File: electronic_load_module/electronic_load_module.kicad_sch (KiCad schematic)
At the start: 71 parts, among them J1 Conn_01x03_Pin, J10 Conn_01x02_Pin, J2 Conn_01x03_Pin, J2 Screw_Terminal_01x02, J3 Conn_01x04_Pin, J6 Conn_01x05_Pin, J7 Conn_01x04_Pin, J8 Conn_01x04_Pin, J9 Conn_01x04_Pin, Q1 TIP142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

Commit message: Image added
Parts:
- V1: now not fitted; now left out of the parts list
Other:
- moved on the sheet: C1, C2, C4, C5, C6, C8, J3, J7, Q2, Q3, R11, R5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

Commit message: IDeo ok
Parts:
- removed C4, C8: 100n, Capacitor_SMD:C_0603_1608Metric_Pad1.08x0.95mm_HandSolder, symbol Device:C
- removed J1: Conn_01x03_Pin, Connector_PinHeader_2.54mm:PinHeader_1x03_P2.54mm_Vertical, symbol Connector:Conn_01x03_Pin
- removed J10: Conn_01x02_Pin, Connector_PinHeader_2.54mm:PinHeader_1x02_P2.54mm_Vertical, symbol Connector:Conn_01x02_Pin
- removed J2: Screw_Terminal_01x02, TerminalBlock:TerminalBlock_Altech_AK300-2_P5.00mm, symbol Connector:Screw_Terminal_01x02
- removed J3, J7, J8, J9: Conn_01x04_Pin, Connector_PinHeader_2.54mm:PinHeader_1x04_P2.54mm_Vertical, symbol Connector:Conn_01x04_Pin
- removed Q3, Q4: BC549, Package_TO_SOT_THT:TO-92_Inline, symbol SPICE_bjts:BC549
- removed R11: 280k, Resistor_SMD:R_0603_1608Metric_Pad0.98x0.95mm_HandSolder, symbol Device:R
- removed R11: 20k, Resistor_SMD:R_0603_1608Metric_Pad0.98x0.95mm_HandSolder, symbol Device:R
- removed R5 (x17): 0, Resistor_SMD:R_0603_1608Metric_Pad0.98x0.95mm_HandSolder, symbol Device:R
- removed R5 (x3): 10k, Resistor_SMD:R_0603_1608Metric_Pad0.98x0.95mm_HandSolder, symbol Device:R
- removed R5 (x2): 1k, Resistor_SMD:R_0603_1608Metric_Pad0.98x0.95mm_HandSolder, symbol Device:R
- removed unit 2 of U1
- removed unit 5 of U1
- removed unit 3 of U1
- removed unit 4 of U1
- removed U2: MCP9700Ax-ETT, Package_TO_SOT_THT:TO-92_Inline, symbol Sensor_Temperature:MCP9700Ax-ETT
- removed unit 1 of U6
- removed V1: 5, symbol Simulation_SPICE:VDC
- added C9 (x3): 100n, Capacitor_SMD:C_0603_1608Metric_Pad1.08x0.95mm_HandSolder, symbol Device:C
- added J10: Conn_01x05_Pin, Connector_JST:JST_EH_B5B-EH-A_1x05_P2.50mm_Vertical, symbol Connector:Conn_01x05_Pin
- added J11: Conn_01x03_Pin, Connector_PinHeader_2.54mm:PinHeader_1x03_P2.54mm_Vertical, symbol Connector:Conn_01x03_Pin
- added J5, J7: Conn_01x03_Pin, Connector_JST:JST_EH_B3B-EH-A_1x03_P2.50mm_Vertical, symbol Connector:Conn_01x03_Pin
- added J8, J9: Conn_01x02_Socket, Connector_JST:JST_EH_B2B-EH-A_1x02_P2.50mm_Vertical, symbol Connector:Conn_01x02_Socket
- added R11: 90k, Resistor_SMD:R_0603_1608Metric_Pad0.98x0.95mm_HandSolder, symbol Device:R
- added R11: 100, Resistor_SMD:R_0603_1608Metric_Pad0.98x0.95mm_HandSolder, symbol Device:R
- added R11: 3.3k, Resistor_SMD:R_0603_1608Metric_Pad0.98x0.95mm_HandSolder, symbol Device:R
- added R11: 6.6k, Resistor_SMD:R_0603_1608Metric_Pad0.98x0.95mm_HandSolder, symbol Device:R
- added R5: 10k, Resistor_SMD:R_0603_1608Metric_Pad0.98x0.95mm_HandSolder, symbol Device:R
- added U2: TLV07, Package_SO:SOIC-8_3.9x4.9mm_P1.27mm, symbol SPICE_opamps:TLV07
- B1, J2, V2, V6: now not fitted; now left out of the parts list
- C2, C7: value 10n -> 100p
- J6: footprint Connector_PinHeader_2.54mm:PinHeader_1x05_P2.54mm_Vertical -> Connector_JST:JST_EH_B5B-EH-A_1x05_P2.50mm_Vertical; Price (none) -> 0.02
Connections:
- net ADC_SHUNT is gone; now on an unnamed net: J2.2 (Pin_2)
- net ADC_SHUNT_2 is gone; now on an unnamed net: U6.14
- net TEMP is gone; now on net COMMON_MUX_B: J6.3 (Pin_3)
- net input_divider is gone; now on an unnamed net: U1.3 (+)
- net 0: now also J6.5 (Pin_5), C9.2, C9.2, C9.2, J10.5 (Pin_5), R5.1, U2.4 (V-)
- net 5V: now also J6.1 (Pin_1), C9.1, C9.1, C9.1, J10.1 (Pin_1), U2.7 (V+)
- net COMMON_MUX_A: now also J6.2 (Pin_2), J10.2 (Pin_2); no longer J6.1 (Pin_1)
- net COMMON_MUX_B: now also J10.3 (Pin_3); no longer J6.2 (Pin_2)
- net DAC: now also U3.2 (Y2), U6.7, J11.1 (Pin_1)
- net DAC_2: now also J2.1 (Pin_1), U5.2 (Y2), U6.8, R5.2; no longer U6.7
- net DAC_from_board: now also J8.1 (Pin_1); no longer J2.1 (Pin_1)
- net DAC_from_board_2: now also J9.1 (Pin_1)
- net DIVIDER: now also U3.15 (X2), U5.15 (X2), J10.4 (Pin_4), U2.2 (-), U2.6; no longer J6.5 (Pin_5), U1.1
- net SHUNT: now also U3.4 (Y3), U3.5 (Y1), J8.2 (Pin_2)
- net SHUNT_2: now also U5.4 (Y3), U5.5 (Y1), J9.2 (Pin_2); no longer U6.12 (+)
- net input_sense: now also J7.1 (Pin_1), R11.1
- net at C7.1, R5.2: now also U6.10 (+); no longer U6.5 (+)
- net at U1.2 (-): now also C1.1, R5.2, U3.3 (Y)
- net at U6.13 (-): now also C5.1, R5.2, U5.3 (Y)
- net at U5.14 (X1): now also U5.11 (X3)
- net at U5.13 (X): now also U6.12 (+); no longer U6.10 (+)
- net at R5.1: now also U6.6 (-)
- net at C5.2, R5.1: no longer U6.8
- net at U3.14 (X1): now also U3.11 (X3), J11.2 (Pin_2)
- net at C2.1, R5.2: now also U6.5 (+)
- net at C1.2, R5.1: now also U1.1
- net at R5.1: now also U6.9 (-); no longer U6.6 (-)
- net ENABLE renamed MIXER
- net MIXER: now also J11.3 (Pin_3), J5.3 (Pin_3)
- new net: J7.3 (Pin_3), R11.2
- new net DIVIDER_R: R11.1, R11.2, U2.3 (+)
- new net input_10: J5.1 (Pin_1), R11.1, R11.2
- new net input_1000: J5.2 (Pin_2), R11.1, R11.2
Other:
- note added: "BJT half"
- note added: "Connector to mixer"
- note added: "Connectors to front panel"
- note added: "Daisy chain"
- note added: "jumpers used to select DAC or MIXER control"
- note added: "omit on the rest of the modules"
- note removed: "10 mV/C"
- note removed: "50 kHz reguliše prilično dobro"
- note removed: "ADD ENABLE"
- note removed: "drop ovog tranzistora je 2V na 8A, strava."
- note removed: "https://novi.kupujemprodajem.com/elektronika-i-komponente/moduli-za-samoizgradnju/mcp4725-i2c-dac-12-bitni-modul/oglas/137304825?filterId=3854618127 Jednom zameniće DAC"
- note removed: "leave blank for additonal modules"
- note removed: "možda dodati ako bi se trimovao offset i gain error koji unosi 1% otpornik."
- note removed: "napajanje će biti neki mali flyback, vrv oni noisy adapteri, treba videti koliko bi šumili"
- note removed: "tlv9061 osetvljiv na promena input napona"
- note removed: "to_control daisy chain"
- moved on the sheet: C1, C2, C3, C5, C6, C7, C9, Q1, Q2, R11, R5, U3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

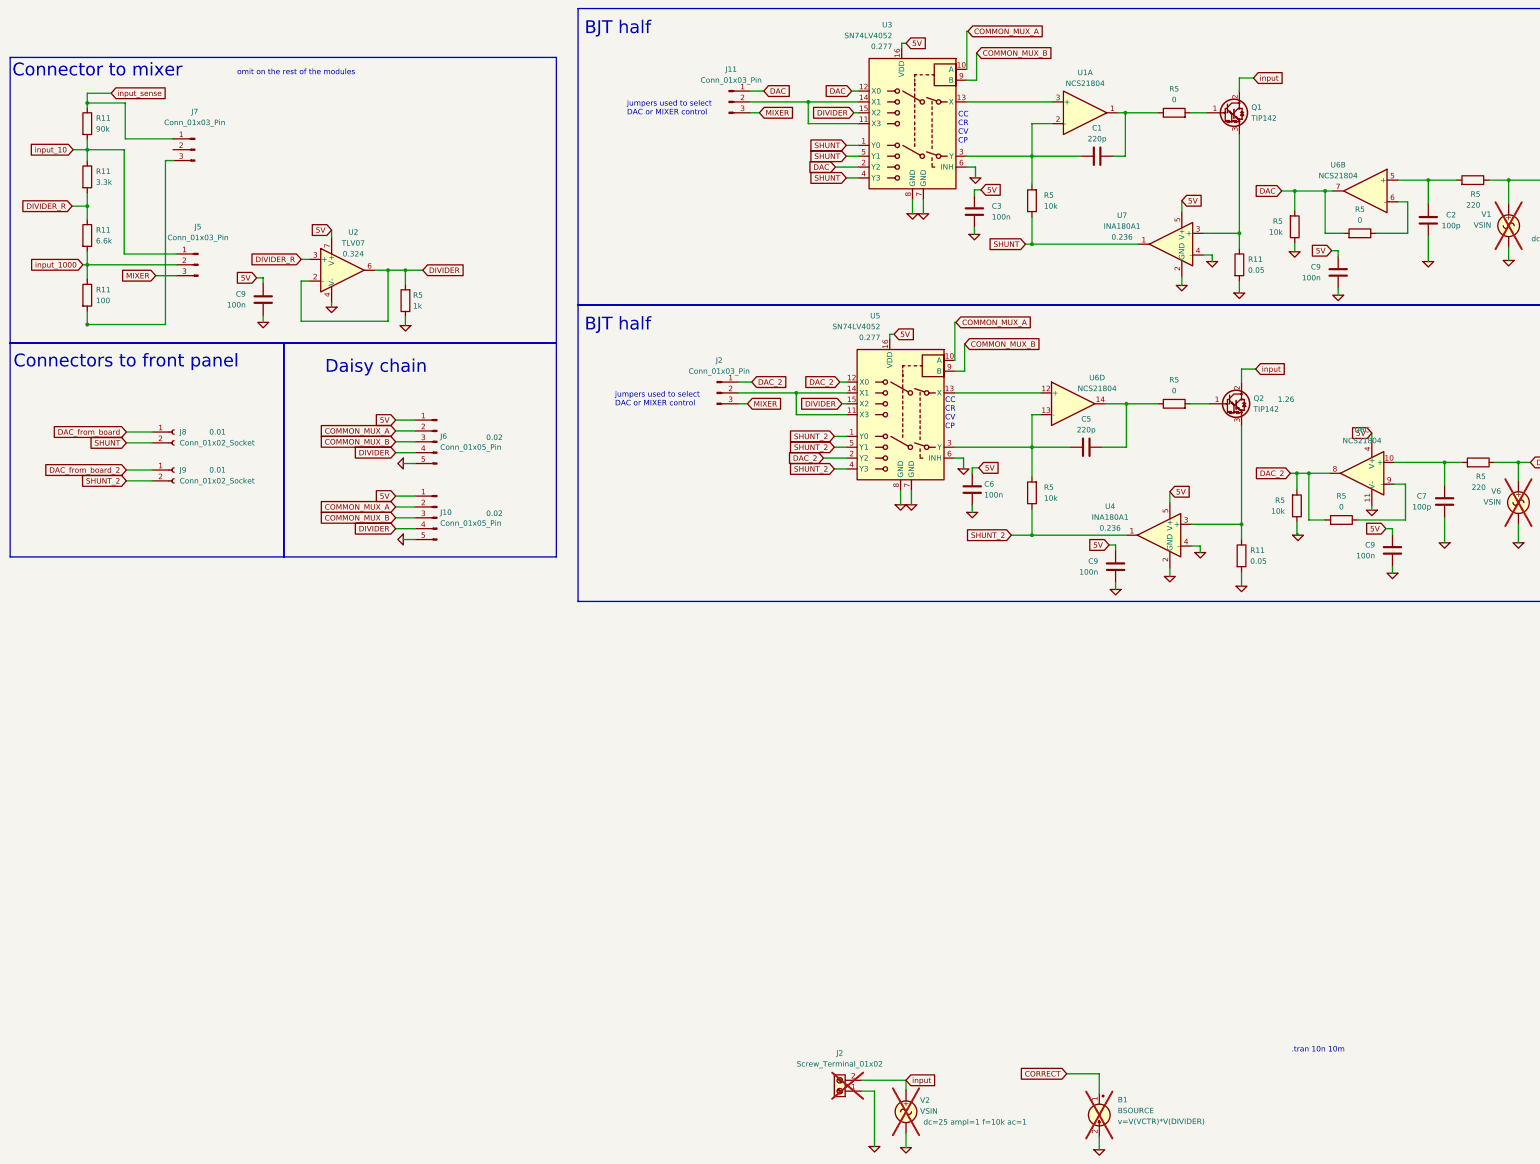
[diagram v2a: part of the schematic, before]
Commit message: Konačno PCB za BJT modul je počeo.
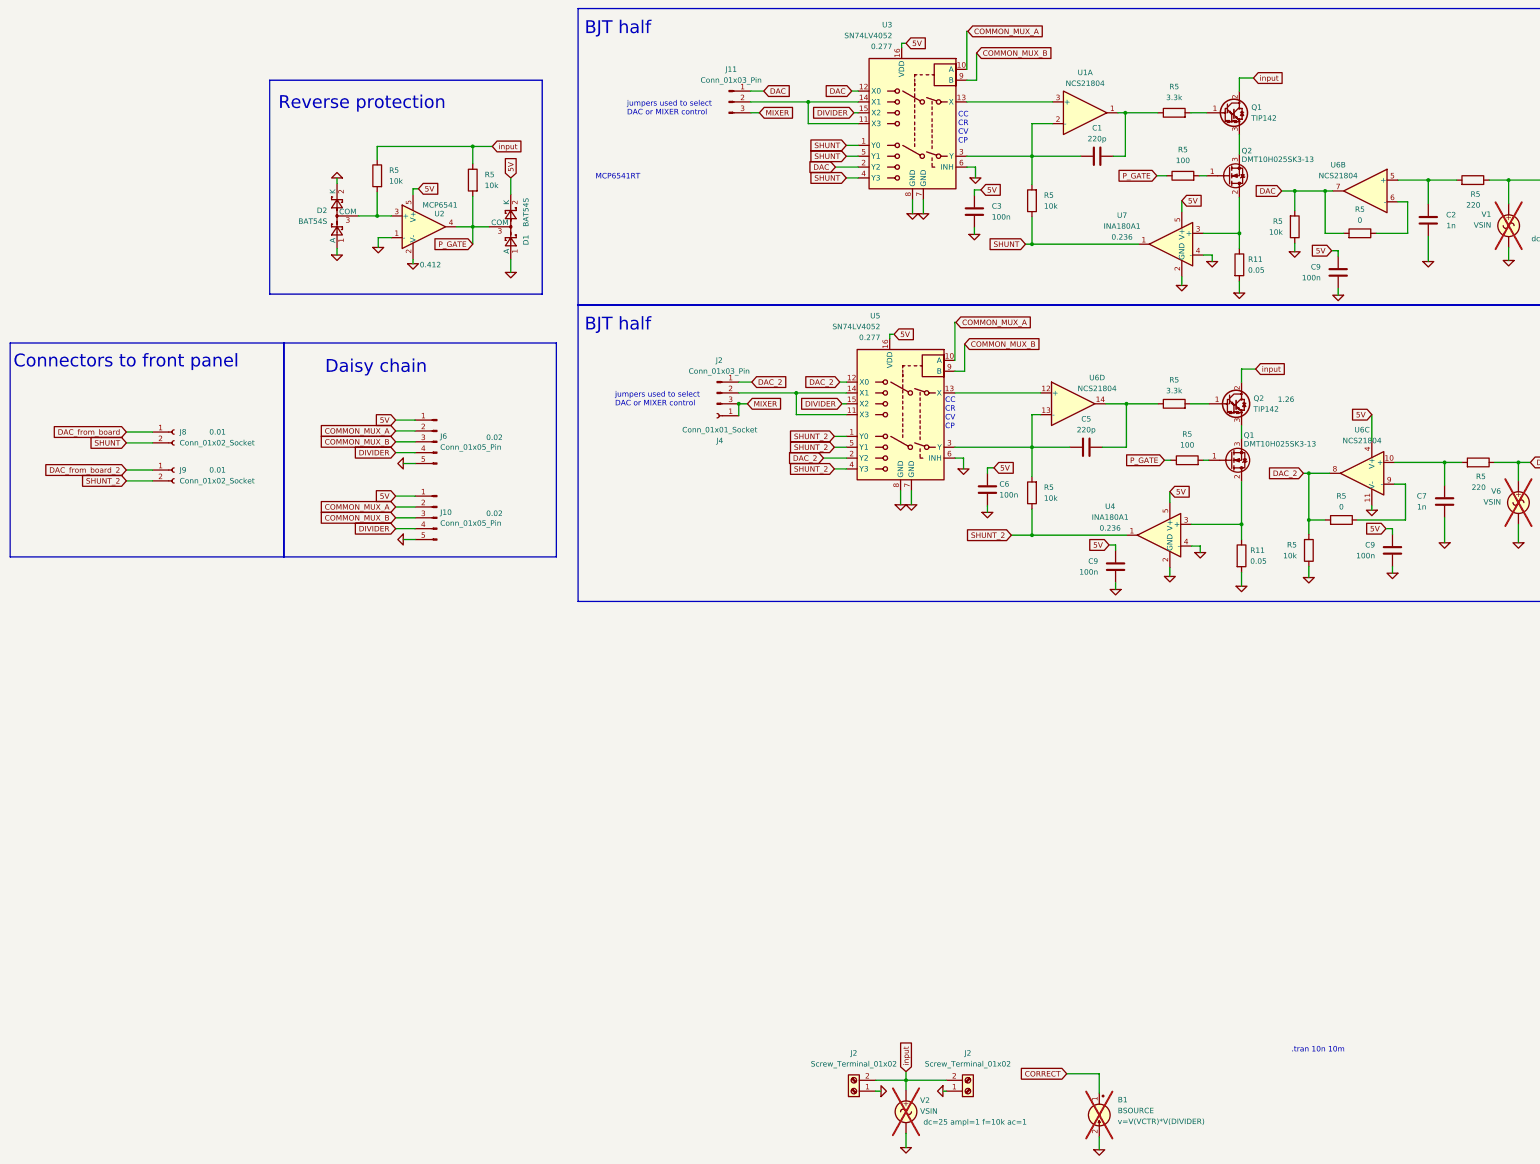
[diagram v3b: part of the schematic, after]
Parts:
- removed C9: 100n, Capacitor_SMD:C_0603_1608Metric_Pad1.08x0.95mm_HandSolder, symbol Device:C
- removed J5, J7: Conn_01x03_Pin, Connector_JST:JST_EH_B3B-EH-A_1x03_P2.50mm_Vertical, symbol Connector:Conn_01x03_Pin
- removed R11: 90k, Resistor_SMD:R_0603_1608Metric_Pad0.98x0.95mm_HandSolder, symbol Device:R
- removed R11: 100, Resistor_SMD:R_0603_1608Metric_Pad0.98x0.95mm_HandSolder, symbol Device:R
- removed R11: 3.3k, Resistor_SMD:R_0603_1608Metric_Pad0.98x0.95mm_HandSolder, symbol Device:R
- removed R11: 6.6k, Resistor_SMD:R_0603_1608Metric_Pad0.98x0.95mm_HandSolder, symbol Device:R
- removed R5: 1k, Resistor_SMD:R_0603_1608Metric_Pad0.98x0.95mm_HandSolder, symbol Device:R
- removed U2: TLV07, Package_SO:SOIC-8_3.9x4.9mm_P1.27mm, symbol SPICE_opamps:TLV07
- added D1, D2: BAT54S, Package_TO_SOT_SMD:SOT-23, symbol SPICE_diodes:BAT54S
- added J2: Screw_Terminal_01x02, TerminalBlock:TerminalBlock_Altech_AK300-2_P5.00mm, symbol Connector:Screw_Terminal_01x02
- added J4: Conn_01x01_Socket, Connector_PinSocket_2.54mm:PinSocket_1x01_P2.54mm_Vertical, symbol Connector:Conn_01x01_Socket
- added Q1, Q2: DMT10H025SK3-13, Package_TO_SOT_SMD:TO-252-2, symbol SPICE_fets:IPD50R380CE
- added R5 (x2): 100, Resistor_SMD:R_0603_1608Metric_Pad0.98x0.95mm_HandSolder, symbol Device:R
- added R5 (x2): 10k, Resistor_SMD:R_0603_1608Metric_Pad0.98x0.95mm_HandSolder, symbol Device:R
- added U2: MCP6541, Package_TO_SOT_SMD:SOT-23-5, symbol SPICE_comparators:TL331
- C2, C7: value 100p -> 1n
- J2: now fitted; now in the parts list
- R5: value 0 -> 3.3k
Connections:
- net 0: now also D1.1 (A), D2.1 (A), D2.2 (K), J2.1 (Pin_1), U2.1 (-), U2.2 (V-)
- net 5V: now also D1.2 (K), U2.5 (V+)
- net MIXER: now also J4.1 (Pin_1)
- net input: now also J2.2 (Pin_2), R5.1, R5.1
- net at R11.1, U7.3 (+): now also Q2.2 (D); no longer Q1.3 (E)
- net at R11.1, U4.3 (+): now also Q1.2 (D); no longer Q2.3 (E)
- new net: Q1.3 (E), Q2.3 (S)
- new net: Q2.1 (G), R5.2
- new net: Q1.3 (S), Q2.3 (E)
- new net: Q1.1 (G), R5.2
- new net: D2.3 (COM), R5.2, U2.3 (+)
- new net P_GATE: D1.3 (COM), R5.1, R5.1, R5.2, U2.4
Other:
- note added: "MCP6541RT"
- note added: "Reverse protection"
- note removed: "Connector to mixer"
- note removed: "omit on the rest of the modules"
- moved on the sheet: C6, R5
